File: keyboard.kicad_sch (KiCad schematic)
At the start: 93 parts, among them J10 Conn_01x13_Pin, J3 Conn_01x13_Pin, SW10 SW_SPST, SW11 SW_SPST, SW12 SW_SPST, SW13 SW_SPST, SW14 SW_SPST, SW15 SW_SPST, SW16 SW_SPST, SW17 SW_SPST, SW18 SW_SPST, SW19 SW_SPST, SW20 SW_SPST, SW21 SW_SPST, SW22 SW_SPST, SW23 SW_SPST, SW24 SW_SPST, SW25 SW_SPST, SW26 SW_SPST, SW27 SW_SPST, SW28 SW_SPST, SW29 SW_SPST, SW3 SW_SPST, SW30 SW_SPST, SW31 SW_SPST, SW32 SW_SPST, SW33 SW_SPST, SW34 SW_SPST, SW35 SW_SPST, SW36 SW_SPST, SW37 SW_SPST, SW38 SW_SPST, SW39 SW_SPST, SW4 SW_SPST, SW5 SW_SPST, SW6 SW_SPST, SW7 SW_SPST, SW8 SW_SPST, SW9 SW_SPST, U17 M110

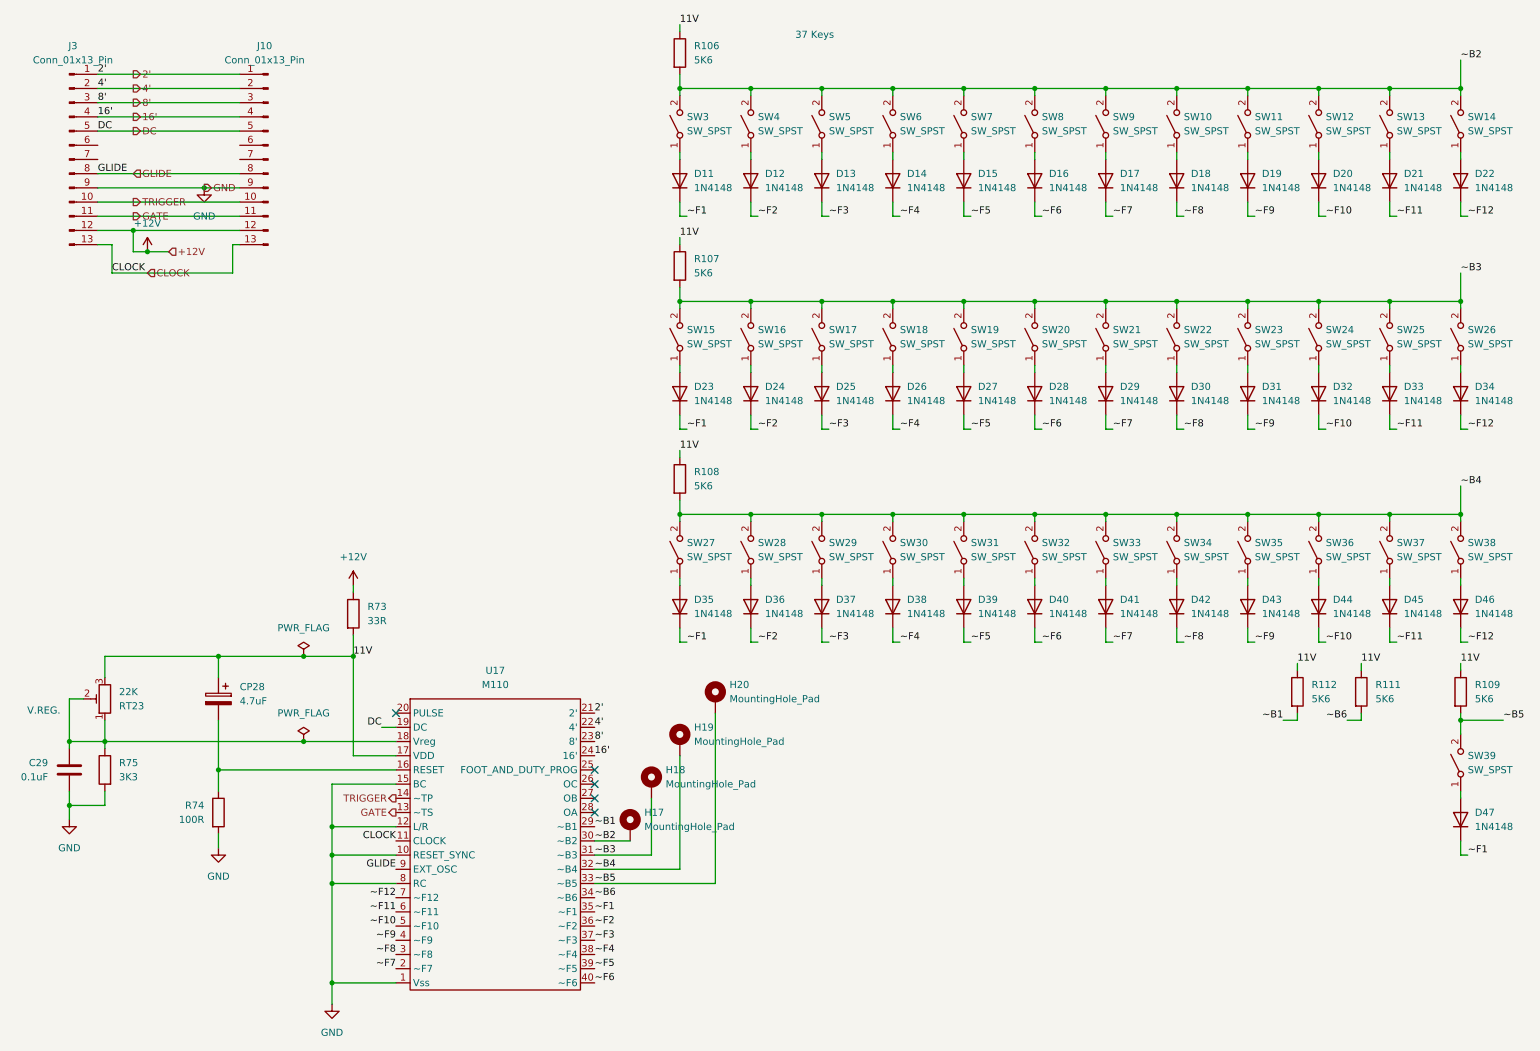
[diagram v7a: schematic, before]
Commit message: Finish keyboard PCB, update power layout
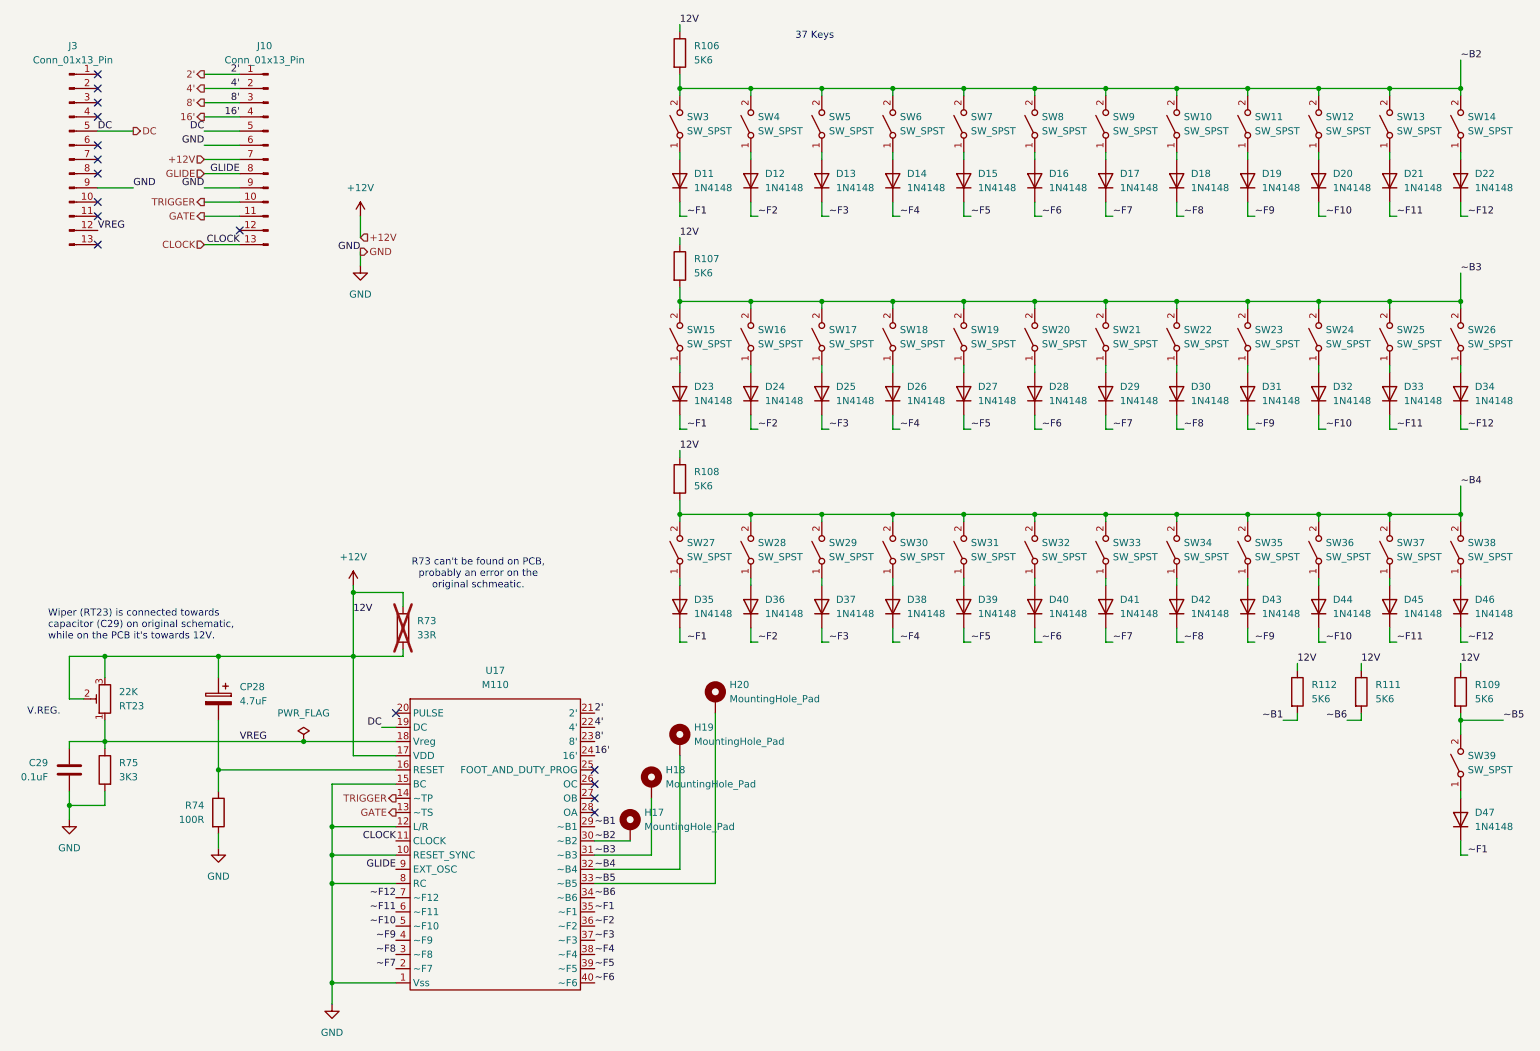
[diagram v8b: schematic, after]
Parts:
- R73: now not fitted
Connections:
- net 11V is gone; now on net +12V: CP28.1, R106.1, R107.1, R108.1, R109.1, R111.1, R112.1, R73.2, RT23.3, U17.17 (VDD)
- net +12V: now also J10.7 (Pin_7), RT23.2; no longer J10.12 (Pin_12), J3.12 (Pin_12)
- net 16': no longer J3.4 (Pin_4)
- net 2': no longer J3.1 (Pin_1)
- net 4': no longer J3.2 (Pin_2)
- net 8': no longer J3.3 (Pin_3)
- net CLOCK: no longer J3.13 (Pin_13)
- net GATE: no longer J3.11 (Pin_11)
- net GLIDE: no longer J3.8 (Pin_8)
- net GND: now also J10.6 (Pin_6)
- net TRIGGER: no longer J3.10 (Pin_10)
- net VREG: now reaches C29.1, R75.1, RT23.1, U17.18 (Vreg)
- net VREG: now also J3.12 (Pin_12); no longer RT23.2
- no-connect marks 5 -> 16
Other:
- note added: "R73 can't be found on PCB, probably an error on the original schmeatic."
- note added: "Wiper (RT23) is connected towards capacitor (C29) on original schematic, while on the PCB it's towards 12V."
